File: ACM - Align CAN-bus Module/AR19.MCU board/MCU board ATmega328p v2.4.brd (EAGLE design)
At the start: 160 x 100 mm, 46 parts, among them IC1 ATMEGA328P-MMH, IC2 MIC5239-5.0YS_TR, IC3 MCP25625-E_ML, J1 AVR_SPI_PROG_3X2NS, U1 CSTNE16M0V530000R0, U2 CSTNE16M0V530000R0

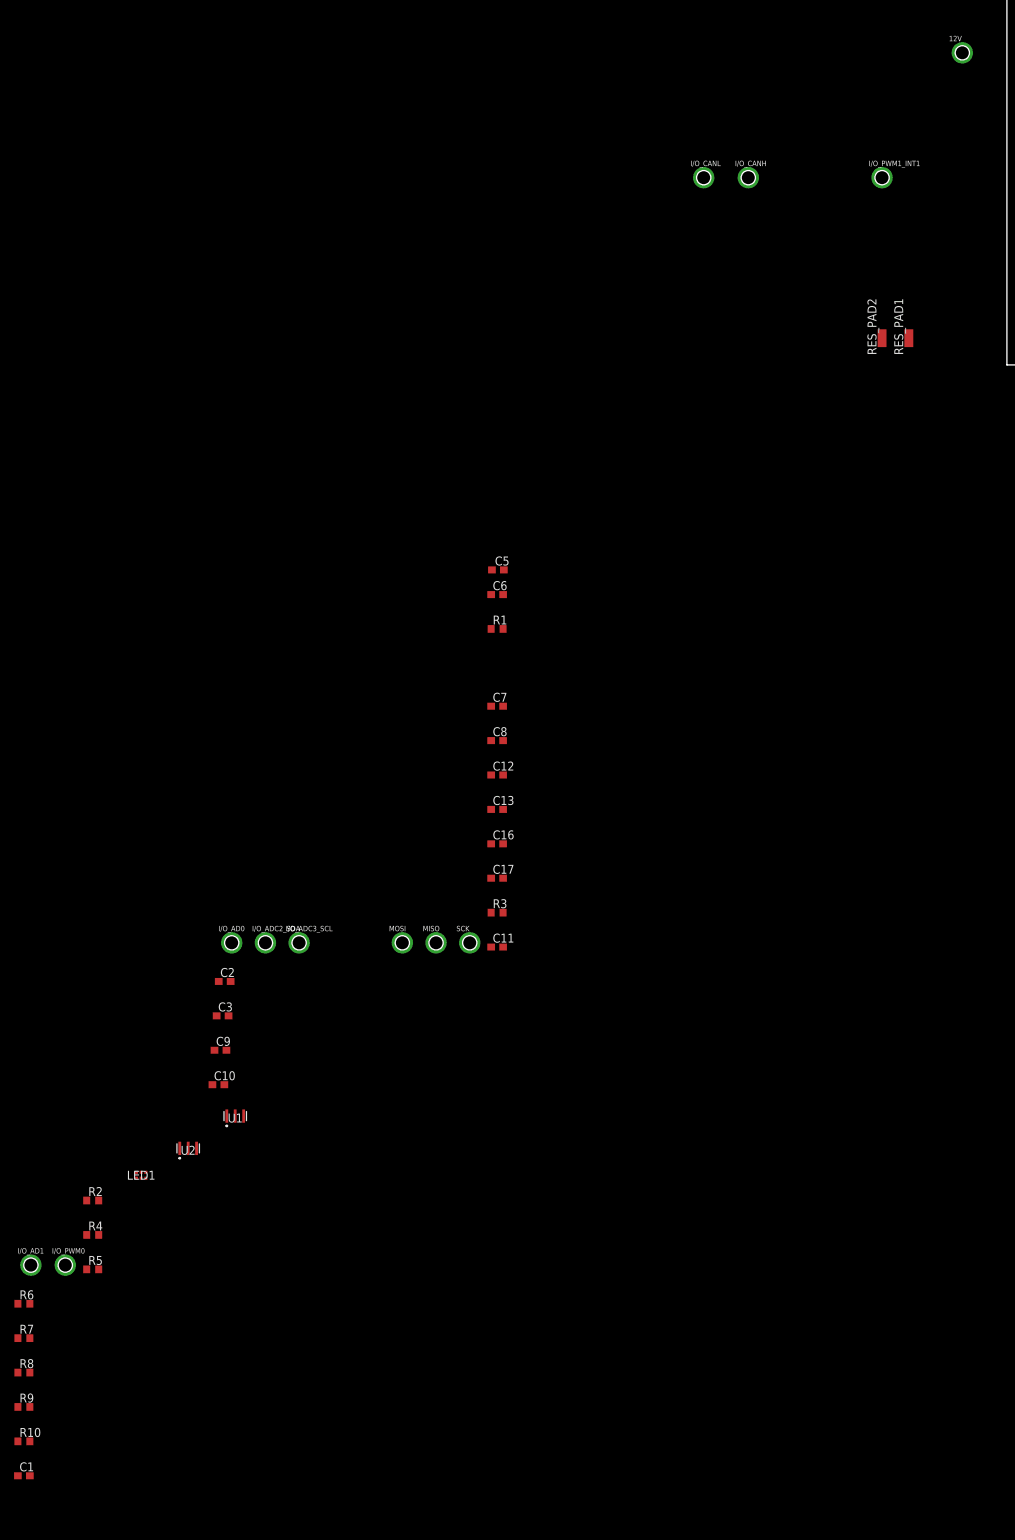
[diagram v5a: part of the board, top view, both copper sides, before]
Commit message: Added GND I/O pin XD
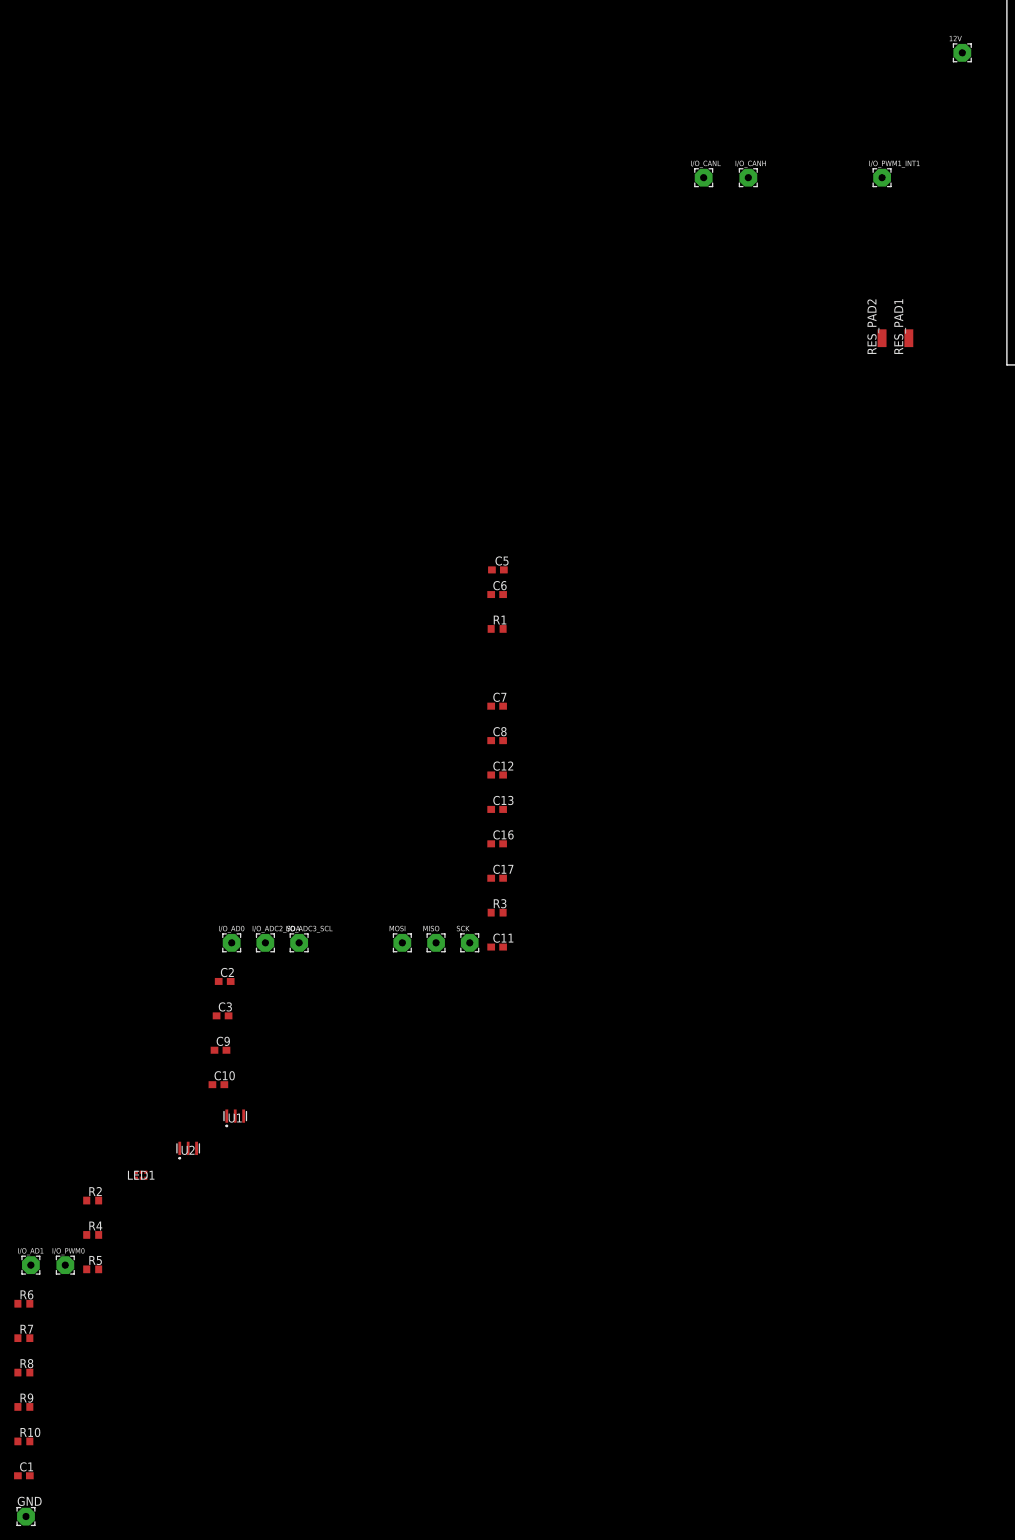
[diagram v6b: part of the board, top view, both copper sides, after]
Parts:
- added GND: GND, wirepad:2,54/1,0
- 12V, I/O_AD0, I/O_AD1, I/O_ADC2_SDA, I/O_ADC3_SCL, I/O_CANH, I/O_CANL, I/O_PWM0, I/O_PWM1_INT1, MISO, MOSI, SCK: device wirepad_edit:2,54/2,0(HALFHOLE)H+V -> wirepad:2,54/1,0
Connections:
- net 12V_UNFUSED: now also 12V.1; no longer 12V.P$1
- net CANH: now also I/O_CANH.1; no longer I/O_CANH.P$1
- net CANL: now also I/O_CANL.1; no longer I/O_CANL.P$1
- net GND: now also GND.1
- net I/O_D2_INT: now also I/O_PWM1_INT1.1; no longer I/O_PWM1_INT1.P$1
- net N$10: now also SCK.1; no longer SCK.P$1
- net N$11: now also MISO.1; no longer MISO.P$1
- net N$12: now also MOSI.1; no longer MOSI.P$1
- net N$2: now also I/O_PWM0.1; no longer I/O_PWM0.P$1
- net N$3: now also I/O_AD1.1; no longer I/O_AD1.P$1
- net N$5: now also I/O_AD0.1; no longer I/O_AD0.P$1
- net N$6: now also I/O_ADC2_SDA.1; no longer I/O_ADC2_SDA.P$1
- net N$7: now also I/O_ADC3_SCL.1; no longer I/O_ADC3_SCL.P$1

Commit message: Voltage divider resistor changed
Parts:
- R10: value 200Ohm -> 2kOhm
- R9: value 200Ohm -> 3kOhm
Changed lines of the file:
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@@
 <attribute name="VALUE" x="-140.635" y="-145.405" size="1.27" layer="27"/>
 </element>
-<element name="R9" library="eagle-ltspice" library_urn="urn:adsk.eagle:library:217" package="R0603" package3d_urn="urn:adsk.eagle:package:13302/1" value="200Ohm" x="-140" y="-148.4">
+<element name="R9" library="eagle-ltspice" library_urn="urn:adsk.eagle:library:217" package="R0603" package3d_urn="urn:adsk.eagle:package:13302/1" value="3kOhm" x="-140" y="-148.4">
 <attribute name="NAME" x="-140.635" y="-147.765" size="1.27" layer="25"/>
 <attribute name="SPICEMODEL" value="NONE" x="-140" y="-148.4" size="1.778" layer="27" display="off"/>
@@
 <attribute name="VALUE" x="-140.635" y="-150.305" size="1.27" layer="27"/>
 </element>
-<element name="R10" library="eagle-ltspice" library_urn="urn:adsk.eagle:library:217" package="R0603" package3d_urn="urn:adsk.eagle:package:13302/1" value="200Ohm" x="-140" y="-153.3">
+<element name="R10" library="eagle-ltspice" library_urn="urn:adsk.eagle:library:217" package="R0603" package3d_urn="urn:adsk.eagle:package:13302/1" value="2kOhm" x="-140" y="-153.3">
 <attribute name="NAME" x="-140.635" y="-152.665" size="1.27" layer="25"/>
 <attribute name="SPICEMODEL" value="NONE" x="-140" y="-153.3" size="1.778" layer="27" display="off"/>
